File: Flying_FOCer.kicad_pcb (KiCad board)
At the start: 6 copper layers, 32.8 x 53.5 mm, 132 parts, among them J1 JST-GH, J2 JST-GH, J3 USB_C_Receptacle_USB2.0_16P, J4 Conn_ARM_SWD_TagConnect_TC203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, J5 JST-GH, U1 TCAN3414, U10 AD8417, U11 LMG2100R026VBNR, U12 AD8417, U14 TLV70033_SOT353, U15 TLV70033_SOT353, U2 TCAN3414, U3 TPSM5601, U4 STM32G474CEUx, U7 LMG2100R026VBNR, U8 AD8417, U9 LMG2100R026VBNR, Y1 32MHz

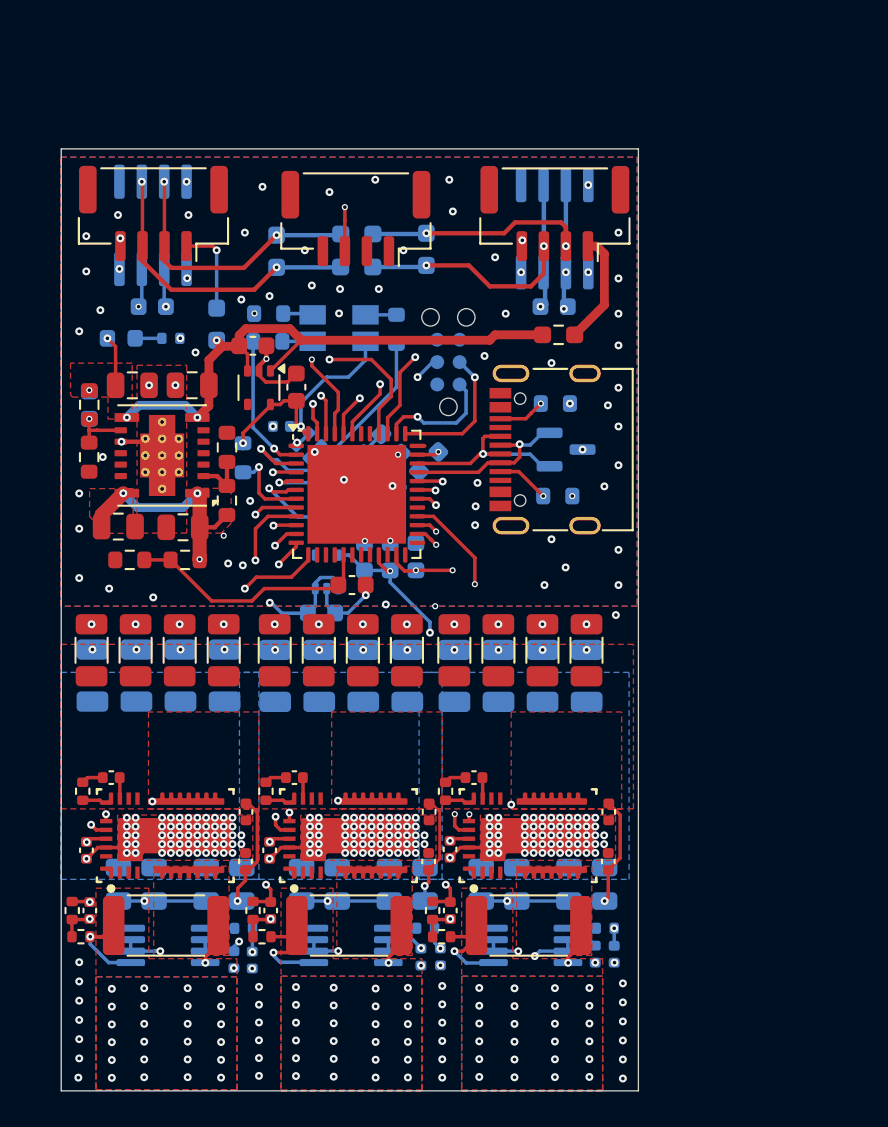
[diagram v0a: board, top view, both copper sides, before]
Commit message: Changed Lib link and added BGA part
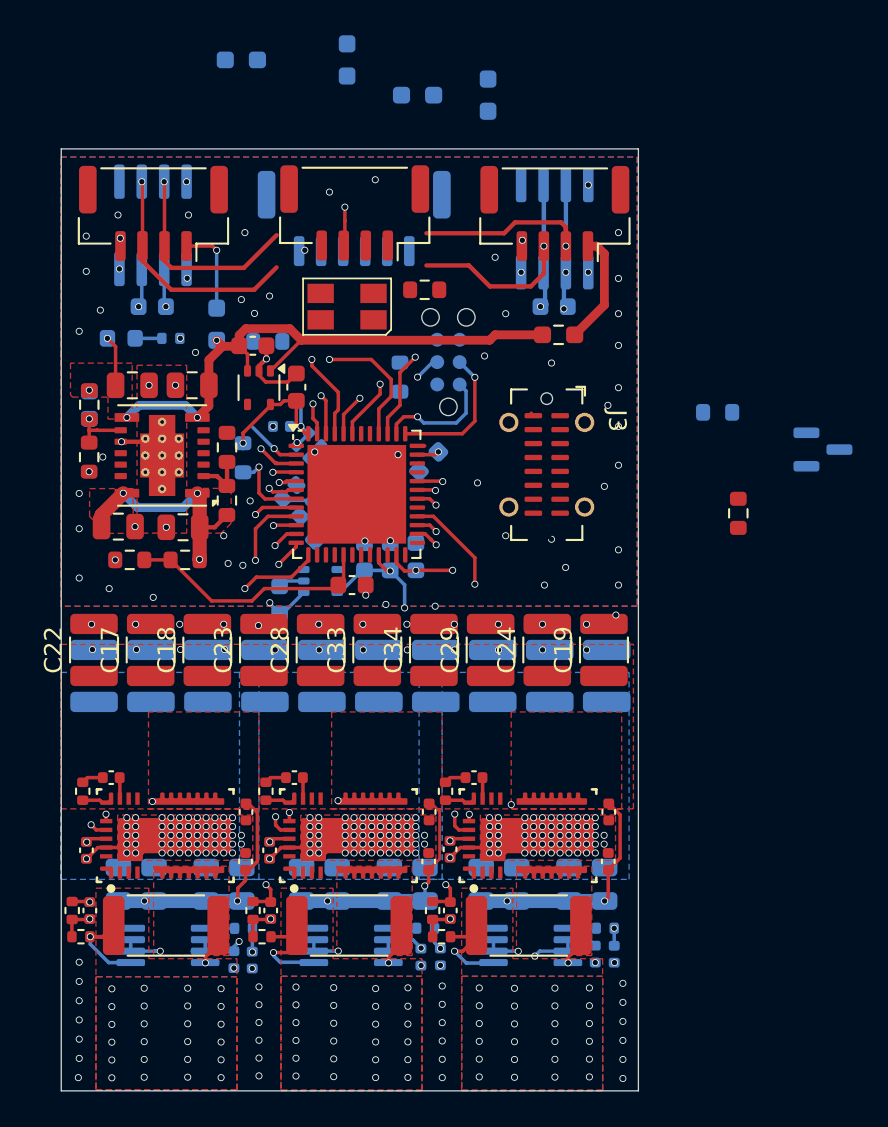
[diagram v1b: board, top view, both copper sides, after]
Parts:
- removed the C38 at (83.4, 90.5)
- removed the C39 at (85.9, 90.5)
- removed the C40 at (88.4, 90.5)
- removed the C41 at (88.4, 92.0)
- removed the C42 at (85.9, 92.0)
- removed the C43 at (80.9, 92.0)
- removed the C44 at (80.9, 90.5)
- removed the C52 at (93.6, 90.5)
- removed the C53 at (98.6, 92.0)
- removed the C54 at (91.1, 92.0)
- removed the C55 at (93.6, 92.0)
- removed the C56 at (91.1, 90.5)
- removed the C57 at (96.1, 92.0)
- removed the C58 at (98.6, 90.5)
- removed the C62 at (78.0, 91.9)
- removed the C63 at (83.4, 92.0)
- removed the C64 at (96.1, 90.5)
- added C15: 10µ, Capacitor_SMD:C_1210_3225Metric, B.Cu at (96.5, 92.0)
- added C16: 10µ, Capacitor_SMD:C_1210_3225Metric, B.Cu at (77.1, 92.0)
- added C17: 10µ, Capacitor_SMD:C_1210_3225Metric, F.Cu at (73.9, 90.5)
- added C18: 10µ, Capacitor_SMD:C_1210_3225Metric, F.Cu at (77.1, 90.5)
- added C19: 10µ, Capacitor_SMD:C_1210_3225Metric, F.Cu at (99.6, 90.5)
- added C20: 10µ, Capacitor_SMD:C_1210_3225Metric, B.Cu at (99.7, 92.0)
- added C21: 10µ, Capacitor_SMD:C_1210_3225Metric, B.Cu at (80.3, 92.0)
- added C22: 10µ, Capacitor_SMD:C_1210_3225Metric, F.Cu at (70.6, 90.5)
- added C23: 10µ, Capacitor_SMD:C_1210_3225Metric, F.Cu at (80.3, 90.5)
- added C31: 10µ, Capacitor_SMD:C_1210_3225Metric, B.Cu at (93.3, 92.0)
- added C32: 10µ, Capacitor_SMD:C_1210_3225Metric, B.Cu at (90.0, 92.0)
- added C33: 10µ, Capacitor_SMD:C_1210_3225Metric, F.Cu at (86.7, 90.5)
- added C34: 10µ, Capacitor_SMD:C_1210_3225Metric, F.Cu at (89.9, 90.5)
- added J1: Conn_01x06, Connector_JST:JST_GH_SM06B-GHS-TB_1x06-1MP_P1.25mm_Horizontal, B.Cu at (85.4, 66.0)
- C24, C30: value 4µ7 -> 10µ; footprint Capacitor_SMD:C_1206_3216Metric -> Capacitor_SMD:C_1210_3225Metric
- C25, C26, C27: value 4µ7 -> 10µ; footprint Capacitor_SMD:C_1206_3216Metric -> Capacitor_SMD:C_1210_3225Metric; moved to B.Cu
- C28, C29: value 4µ7 -> 10µ; footprint Capacitor_SMD:C_1206_3216Metric -> Capacitor_SMD:C_1210_3225Metric; moved to F.Cu
- D4: renamed from D3; moved to F.Cu
- J3: footprint Connector_USB:USB_C_Receptacle_G-Switch_GT-USB-7010ASV -> Connector_USB:USB_C_Receptacle_G-Switch_GT-USB-7051x
- R16: renamed from R17; moved to F.Cu
- R7: moved to F.Cu
- Y1: footprint Crystal:Crystal_SMD_3225-4Pin_3.2x2.5mm -> Crystal:Crystal_SMD_2016-4Pin_2.0x1.6mm
- moved C24 25.9 mm to (96.4, 90.5)
- moved C29 20.1 mm to (93.1, 90.5), turned to 90 degrees
- moved D3 14.6 mm to (112.0, 79.1)
- moved R18 13.5 mm to (79.0, 57.0)
- moved C28 13.0 mm to (83.5, 90.5), turned to 90 degrees
- moved R7 12.1 mm to (107.2, 82.7), turned to 90 degrees
- moved R17 11.6 mm to (85.0, 57.0)
- moved R8 10.2 mm to (106.0, 77.0)
- moved R20 9.42 mm to (93.0, 59.0)
- moved R16 8.96 mm to (89.4, 70.0), turned to 0 degrees
- moved C27 8.92 mm to (86.8, 92.0), turned to -90 degrees
- moved R19 8.60 mm to (89.0, 59.0)
- moved C26 8.20 mm to (83.6, 92.0), turned to -90 degrees
- moved C37 6.20 mm to (83.7, 83.7), turned to 45 degrees
- moved C30 4.91 mm to (70.6, 92.0)
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- renumbered C10 to C1, C4 to C10, C6 to C11, C8 to C12, C9 to C13, C12 to C14, C3 to C2, C34 to C3, C5 to C35, C7 to C36, C14 to C37, C15 to C38, C1 to C39, C48 to C4, C2 to C40, C65 to C41, C22 to C42, C68 to C43, C71 to C44, C74 to C45, C77 to C46, C21 to C47, C23 to C48, C32 to C49, C11 to C5, C33 to C50, C31 to C51, C66 to C52, C36 to C53, C69 to C54, C72 to C55, C75 to C56, C78 to C57, C35 to C58, C37 to C59, C16 to C6, C46 to C60, C47 to C61, C45 to C62, C67 to C63, C50 to C64, C70 to C65, C73 to C66, C76 to C67, C79 to C68, C49 to C69, C17 to C7, C51 to C70, C60 to C71, C61 to C72, C59 to C73, C18 to C8, C19 to C9, D2 to D1, D1 to D3, J5 to J2, J1 to J5, J2 to J6, R33 to R10, R1 to R11, R2 to R12, R15 to R13, R11 to R14, R16 to R15, R4 to R17, R3 to R18, R6 to R19, R9 to R2, R5 to R20, R18 to R21, R19 to R22, R21 to R23, R20 to R24, R22 to R25, R23 to R26, R24 to R27, R26 to R28, R25 to R29, R12 to R3, R27 to R30, R28 to R31, R29 to R32, R31 to R33, R30 to R34, R32 to R35, R10 to R4, R13 to R5, R14 to R6, R34 to R9, U3 to U1, U9 to U10, U10 to U11, U11 to U12, U12 to U13, U14 to U2, U15 to U3, U1 to U5, U2 to U7, U7 to U8, U8 to U9
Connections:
- net /SIGNAL renamed Net-(J2-Pin_1)
- net /TELEM renamed Net-(J2-Pin_2)
- J2 pad 3: /GPIO -> Net-(J2-Pin_3)
- U5 pad 1: /CAN1_RX -> /CAN1_TX
- U5 pad 4: /CAN1_TX -> /CAN1_RX
- U7 pad 1: /CAN2_RX -> /CAN2_TX
- U7 pad 4: /CAN2_TX -> /CAN2_RX
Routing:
- net Net-(U4-PC14): track 15.0 -> 2.34 mm
- net /USB_P: track 11.2 -> 0.00 mm, vias 1 -> 0
- net /USB_N: track 10.0 -> 0.00 mm, vias 1 -> 0
- net Net-(U4-PF0): track 8.69 -> 1.00 mm
- net Net-(U4-PF1): track 8.36 -> 1.66 mm
- net +3v3: track 66.9 -> 61.2 mm
- net Net-(U4-PC13): track 7.98 -> 3.10 mm
- net /CAN1_P: track 15.5 -> 11.8 mm, vias 2 -> 1
- net /CAN1_N: track 17.0 -> 13.3 mm, vias 2 -> 1
- net +5V: track 98.8 -> 95.4 mm
- net /CAN2_N: track 15.6 -> 12.5 mm, vias 2 -> 1
- net /CAN2_P: track 15.9 -> 12.8 mm, vias 2 -> 1
- net Net-(J3-CC1): track 3.01 -> 0.00 mm, vias 1 -> 0
- net Net-(J3-CC2): track 2.65 -> 0.00 mm, vias 1 -> 0
- net Net-(D4-BK): track 1.92 -> 0.00 mm
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- added copper zone on In3.Cu, net GND
